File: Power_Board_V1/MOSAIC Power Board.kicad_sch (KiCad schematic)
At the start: 35 parts, among them J1 CONN E, J10 CONN 2MM JST, J11 CONN 2MM JST, J12 CONN 2MM JST, J13 CONN 2MM JST, J14 CONN 2MM JST, J15 CONN 2MM JST, J16 CONN_JST_BATT, J2 CONN_QWIIC, J3 CONN_JST_BATT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

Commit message: Updated J3, J16 sources
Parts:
- J16, J3: Source https://www.sparkfun.com/products/11641 -> https://www.mouser.com/ProductDetail/485-1769

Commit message: Updatd J2 Source
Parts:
- J2: Source https://www.sparkfun.com/products/14417 -> https://www.mouser.com/ProductDetail/Adafruit/4208?qs=PzGy0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
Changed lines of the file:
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@@
 			)
 		)
-		(property "Source" "https://www.sparkfun.com/products/14417"
+		(property "Source" "https://www.mouser.com/ProductDetail/Adafruit/4208?qs=PzGy0jfpSMtbScLbr0L5dw%3D%3D"
 			(at 21.59 26.67 0)
 			(effects

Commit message: Work on fixing libraries
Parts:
- added H10, H9: MountingHole_Pad, power_board_footprints_V1.0:MountingHole_3.2mm_Pad_Oval, symbol Mechanical:MountingHole_Pad
- added H7, H8: MountingHole_Pad, MountingHole:MountingHole_3.2mm_M3_Pad, symbol Mechanical:MountingHole_Pad
- J10, J11, J12, J13, J14, J15, J4, J5, J6, J7, J8, J9: footprint MOSAIC_main_board_v1.0_footprints:CONN_S2B-PH-SM4-TB_JST -> power_board_footprints_V1.0:CONN_S2B-PH-SM4-TB_JST; symbol MOSAIC_Power_Board:CONN 2mm JST -> power_board_symbols_V1.0:CONN 2mm JST
- U1, U3, U4, U7: footprint MOSAIC_Power_Board:INA219 Breakout -> MOSAIC_main_board_v1.0_footprints:INA219 Breakout; symbol MOSAIC_Power_Board:INA219B_breakout_board -> power_board_symbols_V1.0:INA219B_breakout_board
- U5, U6: footprint MOSAIC_Power_Board:INA219 Breakout -> power_board_footprints_V1.0:INA219 Breakout; symbol MOSAIC_Power_Board:INA219B_breakout_board -> power_board_symbols_V1.0:INA219B_breakout_board
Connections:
- net GND: now also H10.1, H7.1, H8.1, H9.1

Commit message: More fixing of libraries
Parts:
- D1, D2, D3, D4, D5, D6: footprint MOSAIC_Power_Board:D_SOD-323 -> Diode_SMD:D_SOD-323; symbol MOSAIC_Power_Board:B5817WS-TPMSTR-ND -> power_board_symbols_V1.0:B5817WS-TPMSTR-ND
- J1: footprint MOSAIC_Power_Board:M.2-CONNECTOR-E -> power_board_footprints_V1.0:M.2-CONNECTOR-E; symbol MOSAIC_Power_Board:MICROMOD-2222-C -> power_board_symbols_V1.0:MICROMOD-2222-C
- U1, U3, U4, U7: footprint MOSAIC_main_board_v1.0_footprints:INA219 Breakout -> power_board_footprints_V1.0:INA219 Breakout
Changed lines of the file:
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@@
 	)
 	(symbol
-		(lib_id "MOSAIC_Power_Board:B5817WS-TPMSTR-ND")
+		(lib_id "power_board_symbols_V1.0:B5817WS-TPMSTR-ND")
 		(at 189.8904 106.7816 180)
 		(unit 1)
@@
 		(fields_autoplaced yes)
 		(property "Reference" "D5"
-			(at 189.8904 100.2792 0)
+			(at 189.8904 100.33 0)
 			(effects
 				(font
@@
 		)
 		(property "Value" "DIODE SCHOTTKY 20V 1A SOD323"
-			(at 189.8904 102.8192 0)
+			(at 189.8904 102.87 0)
 			(effects
 				(font
@@
 			)
 		)
-		(property "Footprint" "MOSAIC_Power_Board:D_SOD-323"
+		(property "Footprint" "Diode_SMD:D_SOD-323"
 			(at 189.8904 91.7816 0)
 			(effects
@@
 			)
 		)
-		(property "Description" ""
+		(property "Description" "DIODE SCHOTTKY 20V 1A SOD323"
 			(at 189.8904 106.7816 0)
 			(effects
@@
 					(size 1.27 1.27)
 				)
+				(hide yes)
 			)
 		)
@@
 	)
 	(symbol
-		(lib_id "MOSAIC_Power_Board:B5817WS-TPMSTR-ND")
+		(lib_id "power_board_symbols_V1.0:B5817WS-TPMSTR-ND")
 		(at 130.2004 106.7816 180)
 		(unit 1)
@@
 		(fields_autoplaced yes)
 		(property "Reference" "D4"
-			(at 130.2004 100.2792 0)
+			(at 130.2004 100.33 0)
 			(effects
 				(font
@@
 		)
 		(property "Value" "DIODE SCHOTTKY 20V 1A SOD323"
-			(at 130.2004 102.8192 0)
+			(at 130.2004 102.87 0)
 			(effects
 				(font
@@
 			)
 		)
-		(property "Footprint" "MOSAIC_Power_Board:D_SOD-323"
+		(property "Footprint" "Diode_SMD:D_SOD-323"
 			(at 130.2004 91.7816 0)
 			(effects
@@
 			)
 		)
-		(property "Description" ""
+		(property "Description" "DIODE SCHOTTKY 20V 1A SOD323"
 			(at 130.2004 106.7816 0)
 			(effects
@@
 					(size 1.27 1.27)
 				)
+				(hide yes)
 			)
 		)
@@
 	)
 	(symbol
-		(lib_id "MOSAIC_Power_Board:B5817WS-TPMSTR-ND")
+		(lib_id "power_board_symbols_V1.0:B5817WS-TPMSTR-ND")
 		(at 250.2408 107.3404 180)
 		(unit 1)
@@
 		(fields_autoplaced yes)
 		(property "Reference" "D6"
-			(at 250.2408 100.838 0)
+			(at 250.2408 101.6 0)
 			(effects
 				(font
@@
 		)
 		(property "Value" "DIODE SCHOTTKY 20V 1A SOD323"
-			(at 250.2408 103.378 0)
+			(at 250.2408 104.14 0)
 			(effects
 				(font
@@
 			)
 		)
-		(property "Footprint" "MOSAIC_Power_Board:D_SOD-323"
+		(property "Footprint" "Diode_SMD:D_SOD-323"
 			(at 250.2408 92.3404 0)
 			(effects
@@
 			)
 		)
-		(property "Description" ""
+		(property "Description" "DIODE SCHOTTKY 20V 1A SOD323"
 			(at 250.2408 107.3404 0)
 			(effects
@@
 					(size 1.27 1.27)
 				)
+				(hide yes)
 			)
 		)
@@
 			)
 		)
-		(property "Footprint" "MOSAIC_main_board_v1.0_footprints:INA219 Breakout"
+		(property "Footprint" "power_board_footprints_V1.0:INA219 Breakout"
 			(at 90.1192 43.3324 0)
 			(effects
@@
 	)
 	(symbol
-		(lib_id "MOSAIC_Power_Board:MICROMOD-2222-C")
+		(lib_id "power_board_symbols_V1.0:MICROMOD-2222-C")
 		(at 58.42 91.44 0)
 		(unit 1)
@@
 			)
 		)
-		(property "Footprint" "MOSAIC_Power_Board:M.2-CONNECTOR-E"
+		(property "Footprint" "power_board_footprints_V1.0:M.2-CONNECTOR-E"
 			(at 58.42 91.44 0)
 			(effects
@@
 					(size 1.27 1.27)
 				)
+				(hide yes)
 			)
 		)
@@
 	)
 	(symbol
-		(lib_id "MOSAIC_Power_Board:B5817WS-TPMSTR-ND")
+		(lib_id "power_board_symbols_V1.0:B5817WS-TPMSTR-ND")
 		(at 129.54 52.8828 180)
 		(unit 1)
@@
 		(fields_autoplaced yes)
 		(property "Reference" "D1"
-			(at 129.54 46.3804 0)
+			(at 129.54 46.99 0)
 			(effects
 				(font
@@
 		)
 		(property "Value" "DIODE SCHOTTKY 20V 1A SOD323"
-			(at 129.54 48.9204 0)
+			(at 129.54 49.53 0)
 			(effects
 				(font
@@
 			)
 		)
-		(property "Footprint" "MOSAIC_Power_Board:D_SOD-323"
+		(property "Footprint" "Diode_SMD:D_SOD-323"
 			(at 129.54 37.8828 0)
 			(effects
@@
 			)
 		)
-		(property "Description" ""
+		(property "Description" "DIODE SCHOTTKY 20V 1A SOD323"
 			(at 129.54 52.8828 0)
 			(effects
@@
 					(size 1.27 1.27)
 				)
+				(hide yes)
 			)
 		)
@@
 			)
 		)
-		(property "Footprint" "MOSAIC_main_board_v1.0_footprints:INA219 Breakout"
+		(property "Footprint" "power_board_footprints_V1.0:INA219 Breakout"
 			(at 210.1596 43.8912 0)
 			(effects
@@
 			)
 		)
-		(property "Footprint" "MOSAIC_main_board_v1.0_footprints:INA219 Breakout"
+		(property "Footprint" "power_board_footprints_V1.0:INA219 Breakout"
 			(at 149.8092 43.3324 0)
 			(effects
@@
 	)
 	(symbol
-		(lib_id "MOSAIC_Power_Board:B5817WS-TPMSTR-ND")
+		(lib_id "power_board_symbols_V1.0:B5817WS-TPMSTR-ND")
 		(at 249.5804 53.4416 180)
 		(unit 1)
@@
 		(fields_autoplaced yes)
 		(property "Reference" "D3"
-			(at 249.5804 46.9392 0)
+			(at 249.5804 46.99 0)
 			(effects
 				(font
@@
 		)
 		(property "Value" "DIODE SCHOTTKY 20V 1A SOD323"
-			(at 249.5804 49.4792 0)
+			(at 249.5804 49.53 0)
 			(effects
 				(font
@@
 			)
 		)
-		(property "Footprint" "MOSAIC_Power_Board:D_SOD-323"
+		(property "Footprint" "Diode_SMD:D_SOD-323"
 			(at 249.5804 38.4416 0)
 			(effects
@@
 			)
 		)
-		(property "Description" ""
+		(property "Description" "DIODE SCHOTTKY 20V 1A SOD323"
 			(at 249.5804 53.4416 0)
 			(effects
@@
 					(size 1.27 1.27)
 				)
+				(hide yes)
 			)
 		)
@@
 	)
 	(symbol
-		(lib_id "MOSAIC_Power_Board:B5817WS-TPMSTR-ND")
+		(lib_id "power_board_symbols_V1.0:B5817WS-TPMSTR-ND")
 		(at 189.23 52.8828 180)
 		(unit 1)
@@
 		(fields_autoplaced yes)
 		(property "Reference" "D2"
-			(at 189.23 46.3804 0)
+			(at 189.23 46.99 0)
 			(effects
 				(font
@@
 		)
 		(property "Value" "DIODE SCHOTTKY 20V 1A SOD323"
-			(at 189.23 48.9204 0)
+			(at 189.23 49.53 0)
 			(effects
 				(font
@@
 			)
 		)
-		(property "Footprint" "MOSAIC_Power_Board:D_SOD-323"
+		(property "Footprint" "Diode_SMD:D_SOD-323"
 			(at 189.23 37.8828 0)
 			(effects
@@
 			)
 		)
-		(property "Description" ""
+		(property "Description" "DIODE SCHOTTKY 20V 1A SOD323"
 			(at 189.23 52.8828 0)
 			(effects
@@
 					(size 1.27 1.27)
 				)
+				(hide yes)
 			)
 		)
@@
 			)
 		)
-		(property "Footprint" "MOSAIC_main_board_v1.0_footprints:INA219 Breakout"
+		(property "Footprint" "power_board_footprints_V1.0:INA219 Breakout"
 			(at 210.82 97.79 0)
 			(effects
@@
 	)
 	(symbol
-		(lib_name "INA219B_breakout_board_3")
 		(lib_id "power_board_symbols_V1.0:INA219B_breakout_board")
 		(at 93.3196 98.5012 0)
@@
 	)
 	(symbol
-		(lib_name "INA219B_breakout_board_2")
 		(lib_id "power_board_symbols_V1.0:INA219B_breakout_board")
 		(at 153.0096 98.5012 0)

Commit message: Placement and routing work
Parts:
- BT1: footprint MOSAIC_Power_Board:SparkFun Lithium Ion Battery - 6Ah -> power_board_footprints_V1.0:SparkFun Lithium Ion Battery - 2Ah; symbol MOSAIC_Power_Board:Battery -> power_board_symbols_V1.0:Battery; Source https://www.sparkfun.com/products/13856 -> https://www.sparkfun.com/lithium-ion-battery-2ah.html
- J16, J3: footprint MOSAIC_Power_Board:JST-2-SMD -> power_board_footprints_V1.0:JST-2-SMD; symbol MOSAIC_Power_Board:JST_2MM_MALE -> power_board_symbols_V1.0:JST_2MM_MALE
- J2: footprint MOSAIC_Power_Board:JST04_1MM_RA -> power_board_footprints_V1.0:JST04_1MM_RA; symbol MOSAIC_Power_Board:QWIIC_CONNECTOR -> power_board_symbols_V1.0:QWIIC_CONNECTOR
- TP1, TP2: footprint MOSAIC_main_board_v1.0_footprints:PAD.03X.05 -> power_board_footprints_V1.0:PAD.03X.05; symbol MOSAIC_Power_Board:TEST-POINT3X5 -> power_board_symbols_V1.0:TEST-POINT3X5
- U2: footprint MOSAIC_Power_Board:INA219 Breakout -> power_board_footprints_V1.0:INA219 Breakout; symbol MOSAIC_Power_Board:INA219B_breakout_board_1 -> power_board_symbols_V1.0:INA219B_breakout_board
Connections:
- net BATT OUT +: no longer U2.6 (VIN+)
- net SOLAR_IN: no longer U2.5 (VIN-)
- net VIN: no longer U2.1 (VIN)
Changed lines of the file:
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@@
 	)
 	(symbol
-		(lib_id "MOSAIC_Power_Board:QWIIC_CONNECTOR")
+		(lib_id "power_board_symbols_V1.0:QWIIC_CONNECTOR")
 		(at 21.59 26.67 0)
 		(unit 1)
@@
 		(fields_autoplaced yes)
 		(property "Reference" "J2"
-			(at 20.955 16.002 0)
+			(at 20.955 16.51 0)
 			(effects
 				(font
@@
 			)
 		)
-		(property "Footprint" "MOSAIC_Power_Board:JST04_1MM_RA"
+		(property "Footprint" "power_board_footprints_V1.0:JST04_1MM_RA"
 			(at 21.59 26.67 0)
 			(effects
@@
 					(size 1.27 1.27)
 				)
+				(hide yes)
 			)
 		)
@@
 	)
 	(symbol
-		(lib_id "MOSAIC_Power_Board:JST_2MM_MALE")
+		(lib_id "power_board_symbols_V1.0:JST_2MM_MALE")
 		(at 21.59 172.72 90)
 		(unit 1)
@@
 			)
 		)
-		(property "Footprint" "MOSAIC_Power_Board:JST-2-SMD"
+		(property "Footprint" "power_board_footprints_V1.0:JST-2-SMD"
 			(at 21.59 172.72 0)
 			(effects
@@
 					(size 1.27 1.27)
 				)
+				(hide yes)
 			)
 		)
 		(property "Source" "https://www.mouser.com/ProductDetail/485-1769"
-			(at 21.59 172.72 90)
+			(at 21.59 172.72 0)
 			(effects
 				(font
@@
 	)
 	(symbol
-		(lib_name "INA219B_breakout_board_1")
-		(lib_id "MOSAIC_Power_Board:INA219B_breakout_board_1")
+		(lib_id "power_board_symbols_V1.0:INA219B_breakout_board")
 		(at 45.0596 158.1912 0)
 		(unit 1)
@@
 			)
 		)
-		(property "Footprint" "MOSAIC_Power_Board:INA219 Breakout"
-			(at 46.3296 165.8112 0)
+		(property "Footprint" "power_board_footprints_V1.0:INA219 Breakout"
+			(at 42.5196 156.9212 0)
 			(effects
 				(font
@@
 		)
 		(property "Datasheet" "https://learn.adafruit.com/adafruit-ina219-current-sensor-breakout/downloads"
-			(at 46.3296 165.8112 0)
+			(at 42.5196 156.9212 0)
 			(effects
 				(font
@@
 					(size 1.27 1.27)
 				)
+				(hide yes)
 			)
 		)
@@
 	)
 	(symbol
-		(lib_id "MOSAIC_Power_Board:Battery")
+		(lib_id "power_board_symbols_V1.0:Battery")
 		(at 64.77 189.23 0)
 		(unit 1)
@@
 		(fields_autoplaced yes)
 		(property "Reference" "BT1"
-			(at 67.945 187.3885 0)
+			(at 68.58 188.6584 0)
 			(effects
 				(font
@@
 				)
 				(justify left)
+				(hide yes)
 			)
 		)
-		(property "Footprint" "MOSAIC_Power_Board:SparkFun Lithium Ion Battery - 6Ah"
+		(property "Footprint" "power_board_footprints_V1.0:SparkFun Lithium Ion Battery - 2Ah"
 			(at 64.77 187.706 90)
 			(effects
@@
 			)
 		)
-		(property "Datasheet" "https://cdn.sparkfun.com/datasheets/Prototyping/spe-00-DTP605068-3P-6000mah-en-1.0ver.pdf"
+		(property "Datasheet" "~"
 			(at 64.77 187.706 90)
 			(effects
@@
 			)
 		)
-		(property "Description" ""
+		(property "Description" "Multiple-cell battery"
 			(at 64.77 189.23 0)
 			(effects
@@
 					(size 1.27 1.27)
 				)
+				(hide yes)
 			)
 		)
-		(property "Source" "https://www.sparkfun.com/products/13856"
+		(property "Source" "https://www.sparkfun.com/lithium-ion-battery-2ah.html"
 			(at 64.77 189.23 0)
 			(effects
@@
 	)
 	(symbol
-		(lib_id "MOSAIC_Power_Board:TEST-POINT3X5")
+		(lib_id "power_board_symbols_V1.0:TEST-POINT3X5")
 		(at 64.77 180.34 0)
 		(unit 1)
@@
 			)
 		)
-		(property "Footprint" "MOSAIC_main_board_v1.0_footprints:PAD.03X.05"
+		(property "Footprint" "power_board_footprints_V1.0:PAD.03X.05"
 			(at 64.77 180.34 0)
 			(effects
@@
 					(size 1.27 1.27)
 				)
+				(hide yes)
 			)
 		)
@@
 	)
 	(symbol
-		(lib_id "MOSAIC_Power_Board:TEST-POINT3X5")
+		(lib_id "power_board_symbols_V1.0:TEST-POINT3X5")
 		(at 64.77 198.12 0)
 		(unit 1)
@@
 			)
 		)
-		(property "Footprint" "MOSAIC_main_board_v1.0_footprints:PAD.03X.05"
+		(property "Footprint" "power_board_footprints_V1.0:PAD.03X.05"
 			(at 64.77 198.12 0)
 			(effects
@@
 					(size 1.27 1.27)
 				)
+				(hide yes)
 			)
 		)
@@
 	)
 	(symbol
-		(lib_id "MOSAIC_Power_Board:JST_2MM_MALE")
+		(lib_id "power_board_symbols_V1.0:JST_2MM_MALE")
 		(at 40.64 190.5 90)
 		(unit 1)
@@
 			)
 		)
-		(property "Footprint" "MOSAIC_Power_Board:JST-2-SMD"
+		(property "Footprint" "power_board_footprints_V1.0:JST-2-SMD"
 			(at 40.64 190.5 0)
 			(effects
@@
 					(size 1.27 1.27)
 				)
+				(hide yes)
 			)
 		)
 		(property "Source" "https://www.mouser.com/ProductDetail/485-1769"
-			(at 40.64 190.5 90)
+			(at 40.64 190.5 0)
 			(effects
 				(font

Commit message: Placement and routing work
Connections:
- net BATT OUT +: now also U2.6 (VIN+)
- net SOLAR_IN: now also U2.5 (VIN-)
- net VIN: now also U2.1 (VIN)
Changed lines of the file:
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@@
 	(wire
 		(pts
-			(xy 56.9468 160.1724) (xy 56.9468 157.9372)
+			(xy 57.3259 160.2232) (xy 57.3259 157.988)
 		)
 		(stroke
@@
 	(wire
 		(pts
-			(xy 55.5752 160.1724) (xy 56.9468 160.1724)
+			(xy 55.5752 160.2232) (xy 57.3259 160.2232)
 		)
 		(stroke
@@
 	(wire
 		(pts
-			(xy 58.3184 172.8216) (xy 58.3184 180.34)
+			(xy 58.3184 172.7708) (xy 58.3184 180.34)
 		)
 		(stroke
@@
 	(wire
 		(pts
-			(xy 55.5752 172.8216) (xy 58.3184 172.8216)
+			(xy 55.5752 172.7708) (xy 58.3184 172.7708)
 		)
 		(stroke
@@
 	)
 	(label "SOLAR_IN"
-		(at 55.5752 170.2816 0)
+		(at 55.5752 170.2308 0)
 		(effects
 			(font
@@
 	(symbol
 		(lib_id "MOSAIC_Power_Board:VIN")
-		(at 56.9468 157.9372 0)
+		(at 57.3259 157.988 0)
 		(unit 1)
 		(exclude_from_sim no)
@@
 		(dnp no)
 		(property "Reference" "#SUPPLY04"
-			(at 56.9468 157.9372 0)
+			(at 57.3259 157.988 0)
 			(effects
 				(font
@@
 		)
 		(property "Value" "VIN"
-			(at 55.6768 154.1272 0)
+			(at 56.0559 154.178 0)
 			(effects
 				(font
@@
 		)
 		(property "Footprint" ""
-			(at 56.9468 157.9372 0)
+			(at 57.3259 157.988 0)
 			(effects
 				(font
@@
 		)
 		(property "Datasheet" ""
-			(at 56.9468 157.9372 0)
+			(at 57.3259 157.988 0)
 			(effects
 				(font
@@
 		)
 		(property "Description" ""
-			(at 56.9468 157.9372 0)
-			(effects
-				(font
+			(at 57.3259 157.988 0)
+			(effects
+				(font

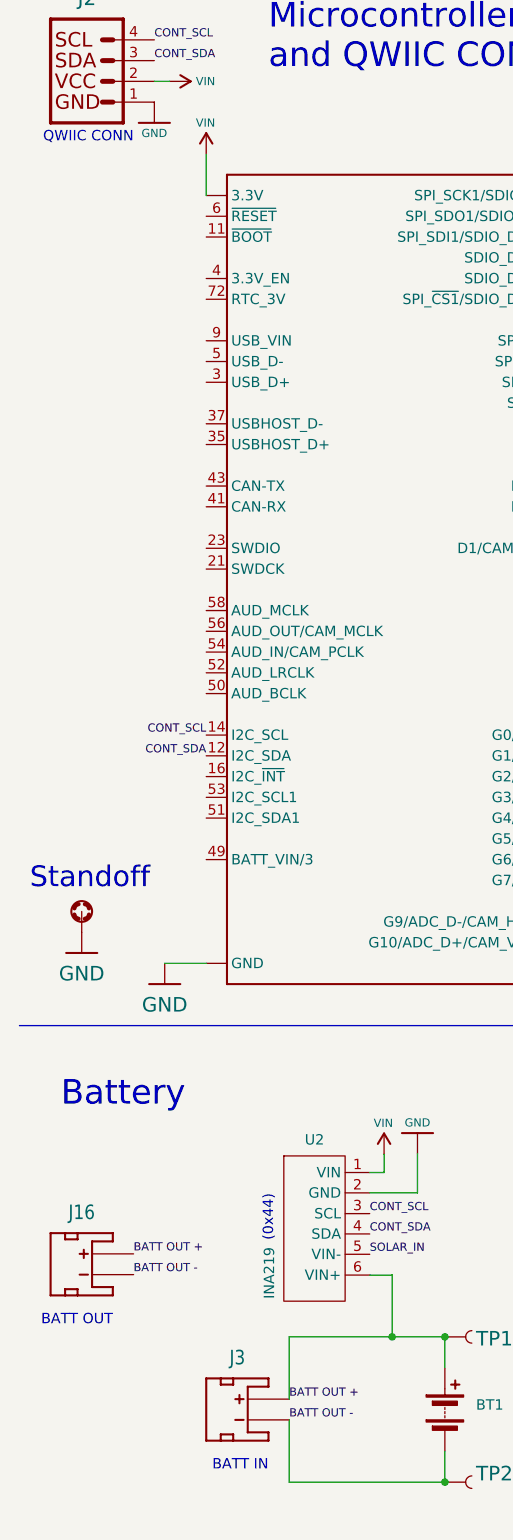
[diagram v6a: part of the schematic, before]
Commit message: Finished placement and tracing
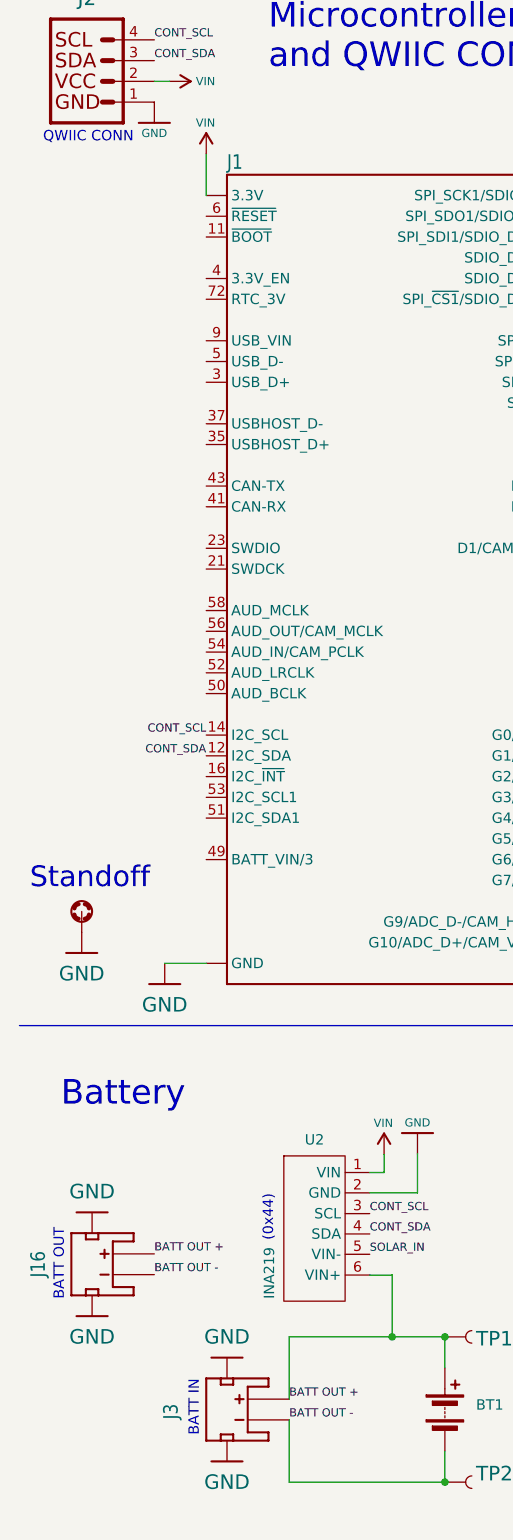
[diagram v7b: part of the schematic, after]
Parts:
- H1: footprint MOSAIC_Power_Board:STAND-OFF-REFLOW-M2.5 -> power_board_footprints_V1.0:STAND-OFF-REFLOW-M2.5; symbol MOSAIC_Power_Board:STAND-OFF-REFLOW-M2.5_2.5MM_TALL -> power_board_symbols_V1.0:STAND-OFF-REFLOW-M2.5_2.5MM_TALL
- J1: JLCPCB Part # (none) -> C2977809; Source https://www.digikey.com/en/products/detail/te-connectivity-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 -> (none)
- J2: JLCPCB Part # (none) -> C145956; Source https://www.mouser.com/ProductDetail/Adafruit/4208?qs=PzGy0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 -> (none)
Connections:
- net GND: now also J16.NC1 (PAD1), J16.NC2 (PAD2), J3.NC1 (PAD1), J3.NC2 (PAD2)
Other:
- moved on the sheet: J16

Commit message: Sourced parts at JLCPCB
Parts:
- D1, D2, D3, D4, D5, D6: JLCPCB Part # (none) -> C435857; Source https://www.digikey.com/en/products/detail/micro-commercial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 -> (none)
- J10, J11, J12, J13, J14, J15, J4, J5, J6, J7, J8, J9: JLCPCB Part # (none) -> C295747; Source https://www.digikey.com/en/products/detail/jst-sales-americ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 -> (none)
